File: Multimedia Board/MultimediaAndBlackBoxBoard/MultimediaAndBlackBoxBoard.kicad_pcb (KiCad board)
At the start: 2 copper layers, 124.5 x 79.2 mm, 37 parts, among them J1 104031-0811, U1 OKI, U2 OKI, U3 BDJ2GA5WEFJ, U4 DS1307Z+, U5 4050, U6 Raspberry_Pi, Y1 32.768KHz

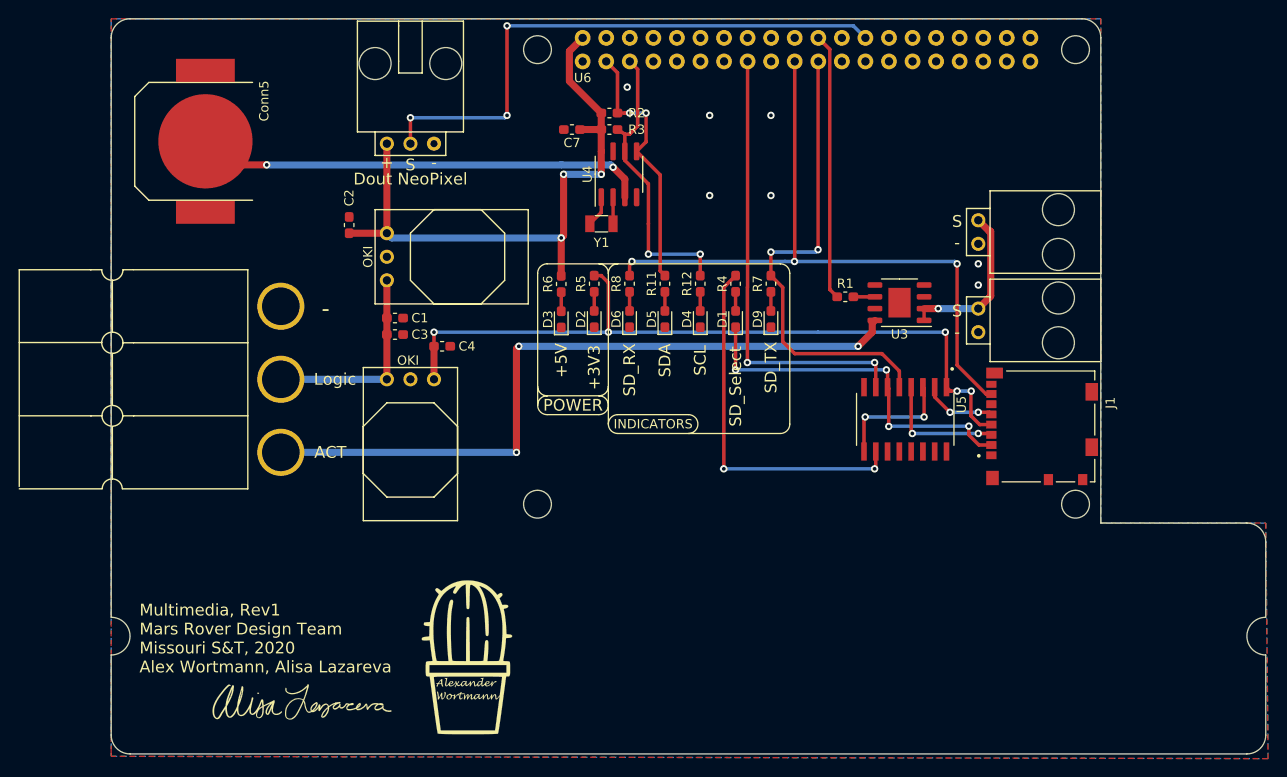
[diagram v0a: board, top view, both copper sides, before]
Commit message: SCLK added for SPI, tags renamed appropriately
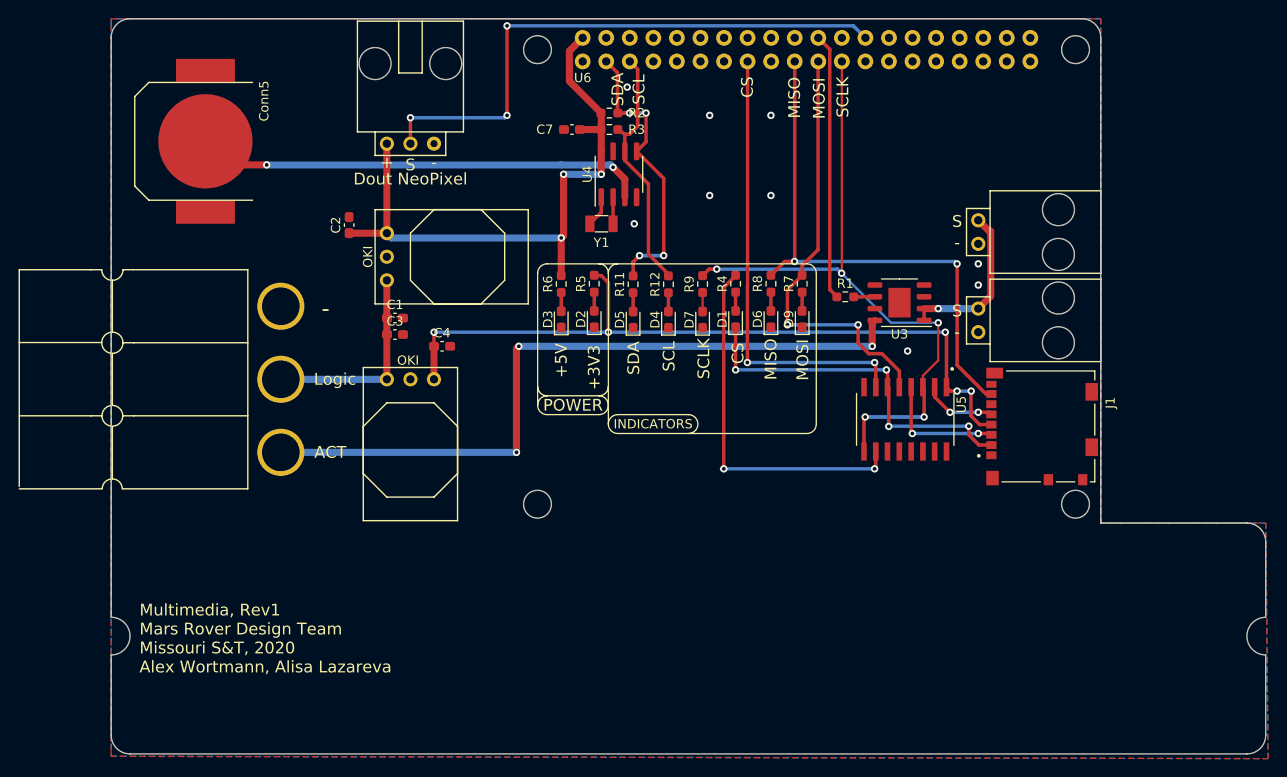
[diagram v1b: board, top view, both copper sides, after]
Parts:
- removed G***: LOGO, Sigs:PricklySig
- removed G***: LOGO, Sigs:Alisa_Lazareva_21mmx9mm
- added D7: BLUE, LED_SMD:LED_0603_1608Metric_Pad1.05x0.95mm_HandSolder, F.Cu at (159.5, 74.9)
- added R9: 330, Resistor_SMD:R_0603_1608Metric_Pad0.98x0.95mm_HandSolder, F.Cu at (159.5, 71.0)
- C1, C2, C3, C4, C7: footprint Capacitor_SMD:C_0603_1608Metric_Pad1.05x0.95mm_HandSolder -> Capacitor_SMD:C_0603_1608Metric_Pad1.08x0.95mm_HandSolder
- R1, R11, R12, R2, R3, R4, R5, R6: footprint Resistor_SMD:R_0603_1608Metric_Pad1.05x0.95mm_HandSolder -> Resistor_SMD:R_0603_1608Metric_Pad0.98x0.95mm_HandSolder
- R7, R8: value 480 -> 330; footprint Resistor_SMD:R_0603_1608Metric_Pad1.05x0.95mm_HandSolder -> Resistor_SMD:R_0603_1608Metric_Pad0.98x0.95mm_HandSolder
- moved D6 15.2 mm to (166.9, 74.8)
- moved R8 15.2 mm to (166.9, 71.0)
- moved D4 3.43 mm to (155.8, 74.9)
- moved D5 3.43 mm to (152.0, 74.9)
- moved R11 3.43 mm to (152.0, 71.0)
- moved R12 3.43 mm to (155.8, 71.0)
- moved D9 3.37 mm to (170.2, 74.8)
- moved R7 3.37 mm to (170.2, 71.0)
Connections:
- net SD_RX renamed SD_MISO
- net SD_TX renamed SD_MOSI
- U5 pad 3: Net-(U5-Pad3) -> SD_SCLK
- U5 pad 9: Net-(U5-Pad3) -> SD_SCLK
- U6 pad 23: Net-(U6-Pad23) -> SD_SCLK
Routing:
- net SD_SCLK: track 0.00 -> 71.9 mm, vias 0 -> 5
- net SD_MISO: track 74.3 -> 58.2 mm, vias 3 -> 2
- net Net-(U5-Pad3): track 13.4 -> 0.00 mm, vias 2 -> 0
- net SCL: track 31.9 -> 27.2 mm, vias 2 -> 0
- net SD_MOSI: track 51.3 -> 46.8 mm
- net SDA: track 28.4 -> 31.2 mm, vias 2 -> 4
- net Net-(D7-Pad2): track 0.00 -> 2.05 mm
- net +12VA: track 77.1 -> 77.9 mm
- net GND: vias 7 -> 9
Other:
- board text added: "CS"
- board text added: "MISO"
- board text added: "MOSI"
- board text added: "SCLK"
- board text removed: "SD_RX"
- board text removed: "SD_Select"
- board text removed: "SD_TX"

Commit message: silkscreen finished
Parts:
- added G***: LOGO, Multimedia:PricklySig(1), F.Cu at (105.7, 109.2)
- added G***: LOGO, Multimedia:Alisa_Lazareva_21mmx9mm, F.Cu at (145.8, 116.3)
